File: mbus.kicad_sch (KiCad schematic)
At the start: 7 parts

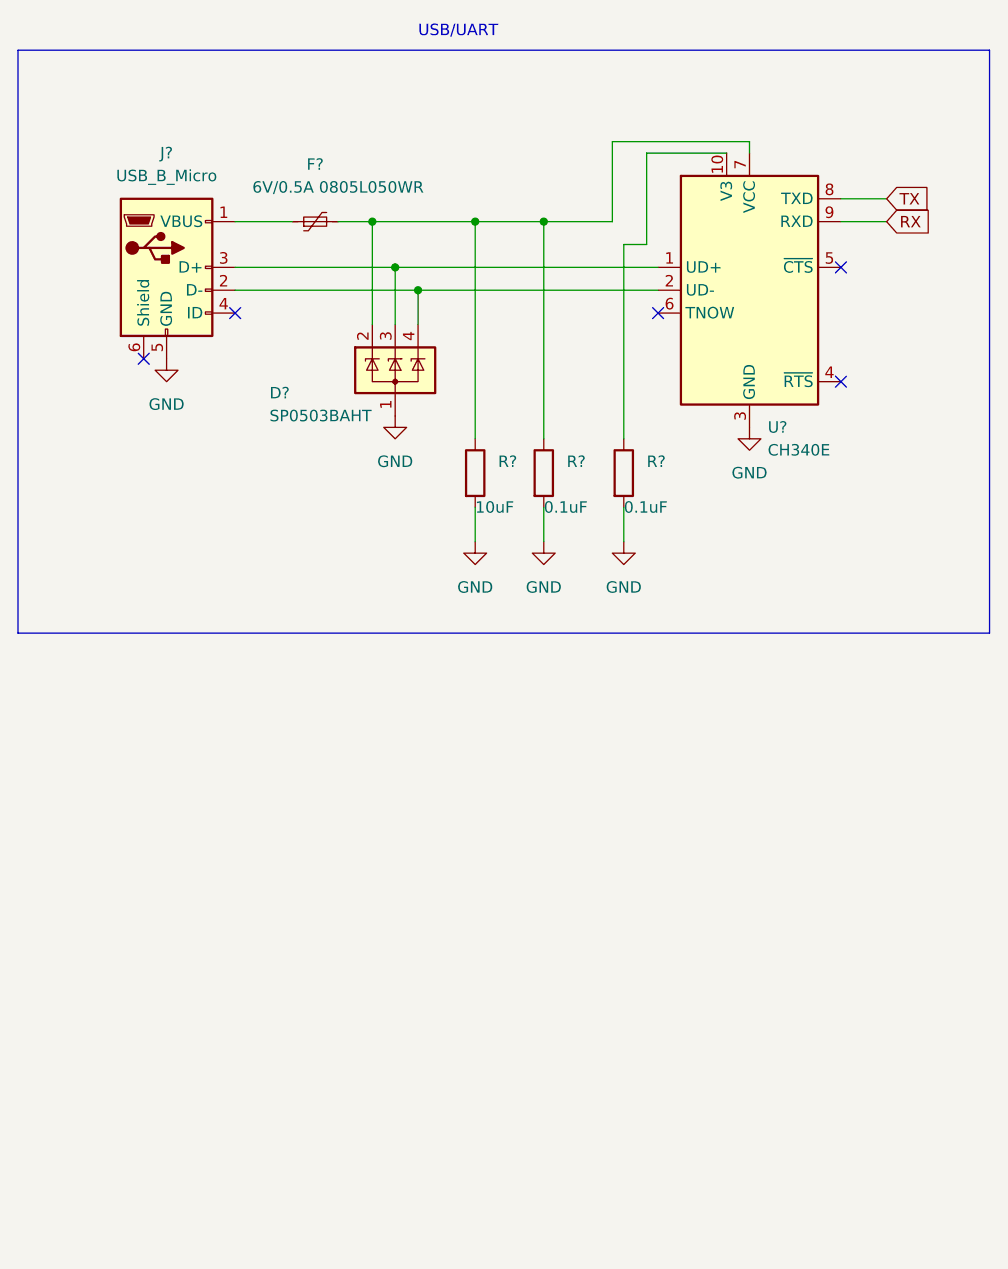
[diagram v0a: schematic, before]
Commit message: mbus driving logic WIP
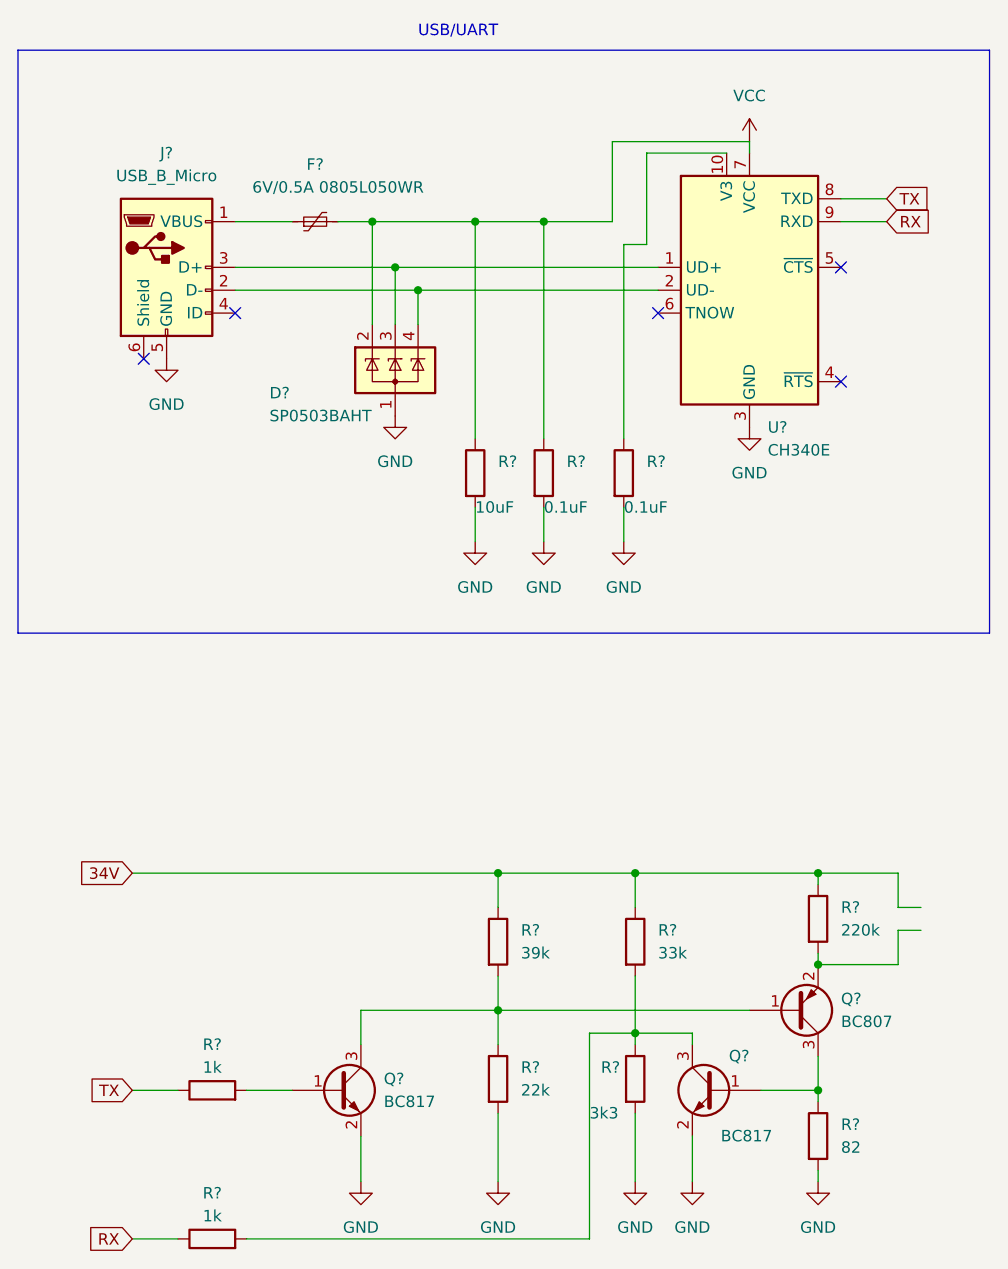
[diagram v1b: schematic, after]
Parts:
- added Q? (x2): BC817, Package_TO_SOT_SMD:SOT-23, symbol Transistor_BJT:BC817
- added Q?: BC807, Package_TO_SOT_SMD:SOT-23, symbol Transistor_BJT:BC807
- added R?: 220k, symbol Device:R
- added R?: 3k3, symbol Device:R
- added R?: 39k, symbol Device:R
- added R?: 22k, symbol Device:R
- added R?: 33k, symbol Device:R
- added R?: 82, symbol Device:R
- added R? (x2): 1k, symbol Device:R
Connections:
- net GND: now also Q?.2 (E), Q?.2 (E), R?.2, R?.2, R?.2
- net RX: now also R?.1
- net TX: now also R?.1
- net VCC: now reaches D?.2 (K), F?.2, R?.1, R?.1, U?.7 (VCC)
- new net: Q?.2 (E), R?.2
- new net: Q?.3 (C), R?.1, R?.2, R?.2
- new net: Q?.1 (B), Q?.3 (C), R?.1, R?.2
- new net: Q?.1 (B), Q?.3 (C), R?.1
- new net: Q?.1 (B), R?.2
- new net 34V: R?.1, R?.1, R?.1

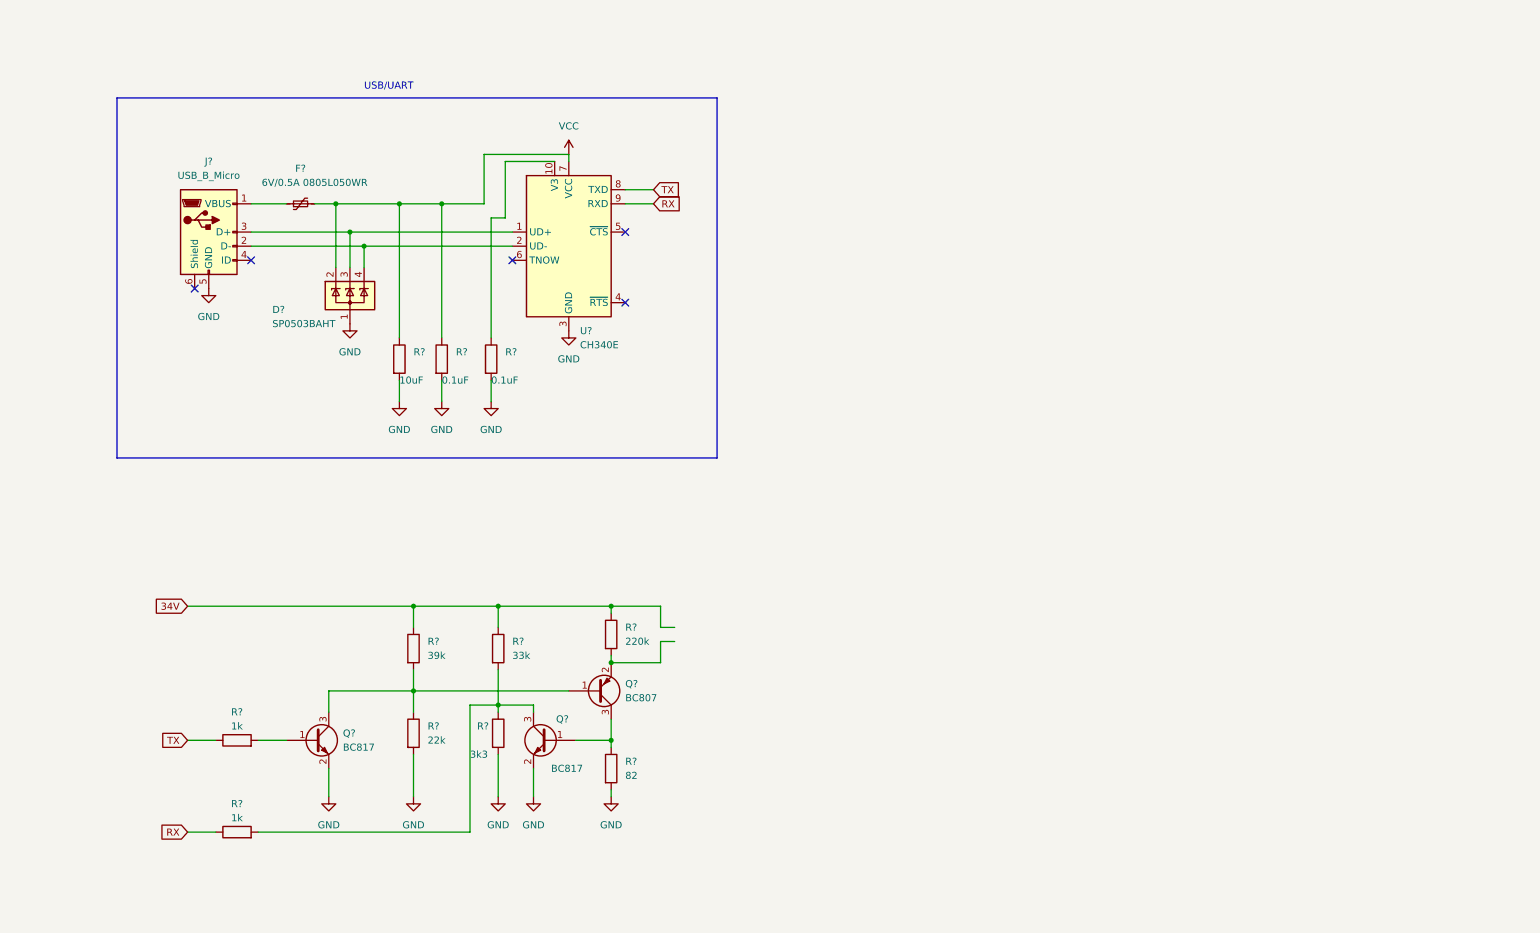
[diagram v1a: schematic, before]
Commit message: Added boost converter, protection components for mbus
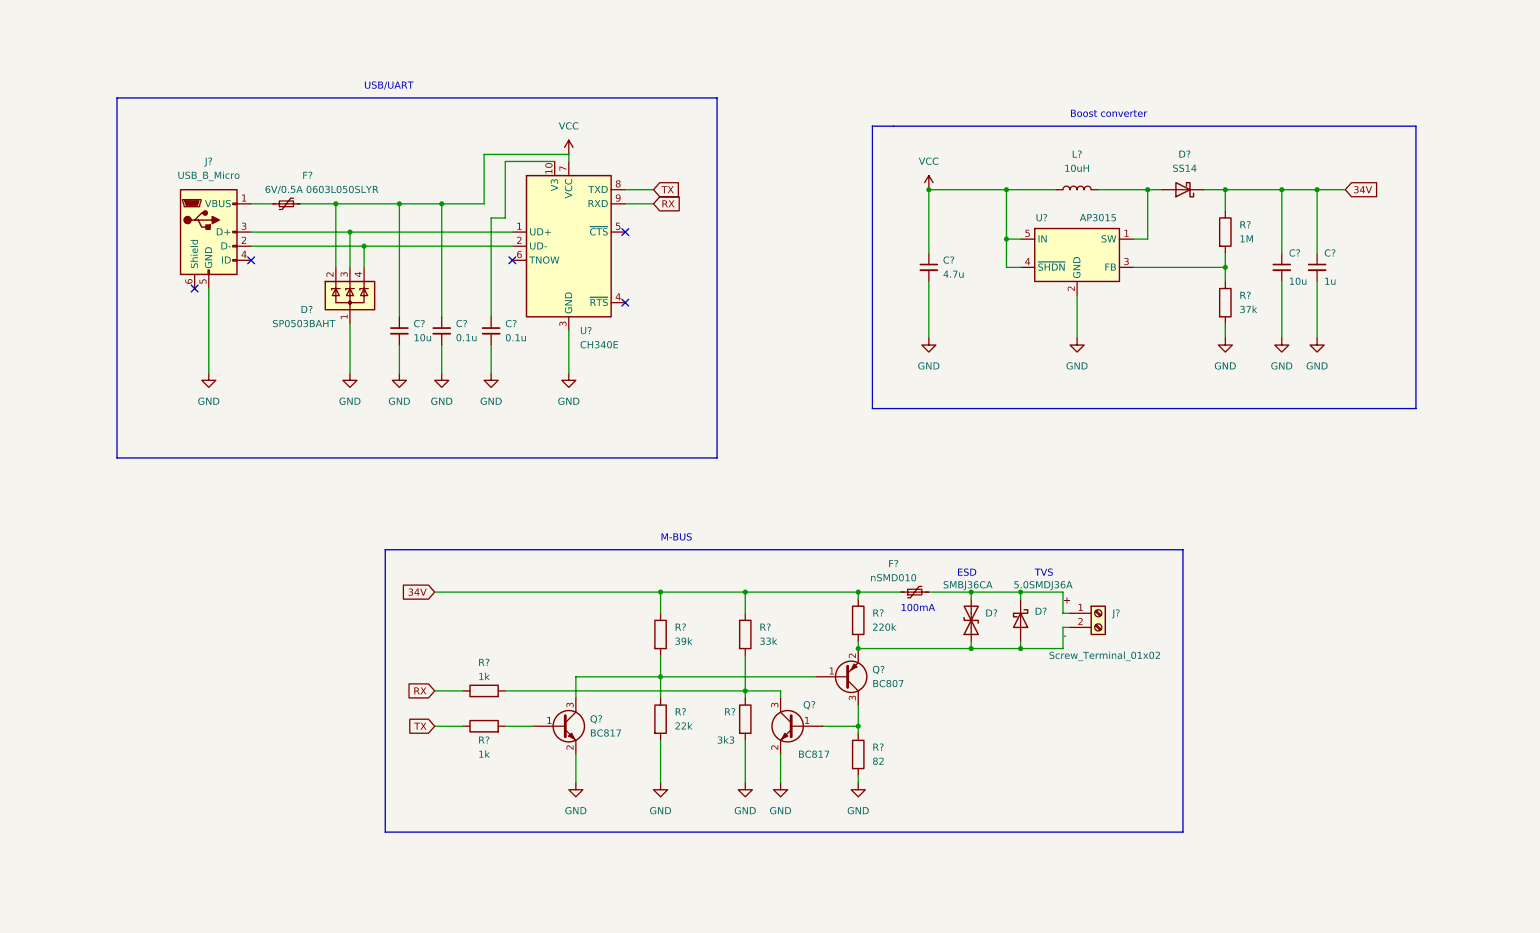
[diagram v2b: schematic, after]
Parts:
- removed R?: 10uF, symbol Device:R
- removed R? (x2): 0.1uF, symbol Device:R
- added C?: 4.7u, symbol Device:C_Small
- added C? (x2): 0.1u, symbol Device:C_Small
- added C? (x2): 10u, symbol Device:C_Small
- added C?: 1u, symbol Device:C_Small
- added D?: SMBJ36CA, symbol Device:D_TVS
- added D?: 5.0SMDJ36A, symbol Device:D_Schottky
- added D?: SS14, symbol Device:D_Schottky
- added F?: nSMD010, symbol Device:Polyfuse_Small
- added J?: Screw_Terminal_01x02, symbol Connector:Screw_Terminal_01x02
- added L?: 10uH, symbol Device:L
- added R?: 37k, symbol Device:R
- added R?: 1M, symbol Device:R
- added U?: AP3015, Package_TO_SOT_SMD:SOT-23-5, symbol mbus_lib:AP3015
- F?: value 6V/0.5A 0805L050WR -> 6V/0.5A 0603L050SLYR
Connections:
- net 34V: now also C?.1, C?.1, D?.1 (K), F?.1, R?.1
- net GND: now also C?.2, C?.2, C?.2, C?.2, C?.2, C?.2, R?.2, U?.2 (GND)
- net VCC: now also C?.1, C?.1, C?.1, L?.1, U?.4 (~{SHDN}), U?.5 (IN)
- net -: now reaches Q?.2 (E), R?.2
- net -: now also D?.1 (A1), D?.2 (A), J?.2 (Pin_2)
- net at U?.10 (V3): now also C?.1
- new net: D?.2 (A), L?.2, U?.1 (SW)
- new net: R?.1, R?.2, U?.3 (FB)
- new net +: D?.1 (K), D?.2 (A2), F?.2, J?.1 (Pin_1)
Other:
- note added: "100mA"
- note added: "Boost converter"
- note added: "ESD"
- note added: "M-BUS"
- note added: "TVS"
- moved on the sheet: F?, Q?, R?

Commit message: Generated designators
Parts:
- F1: renamed from F?; value 6V/0.5A 0603L050SLYR -> 0603L050SLYR
- J2: renamed from J?; value Screw_Terminal_01x02 -> MBUS
- gave numbers to parts that had none: 28
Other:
- note added: "500mA"

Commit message: Replaced 500mA VBUS fuse with 200mA, changed MBUS circuit to work with 5V logic
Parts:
- C1, C2, C3, C4, C5, C6: footprint (none) -> Capacitor_SMD:C_0603_1608Metric
- F1: value 0603L050SLYR -> (none)
- R2: value 1k -> (none)
- R6: value 3k3 -> (none)
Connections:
- net VCC renamed +5V
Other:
- note added: "200mA"
- note added: "R2: 1k"
- note added: "R6: 3k3"
- note added: "Replace these for 3.3V logic levels:"
- note removed: "500mA"

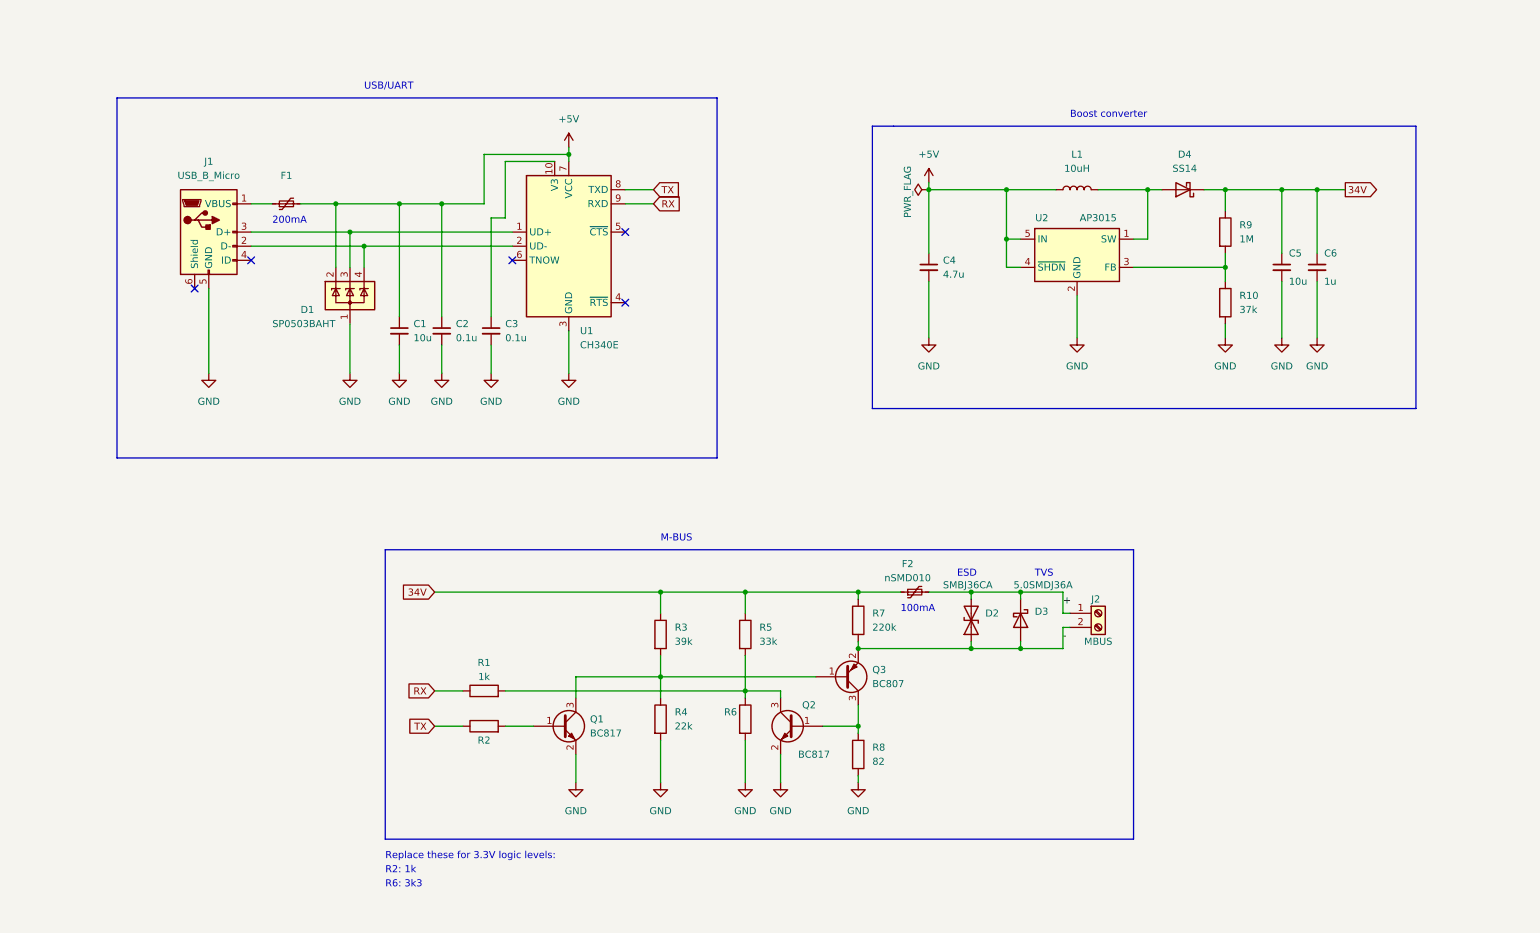
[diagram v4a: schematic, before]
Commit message: Added part numbers, schematic to readme and symbol for mbus power rail
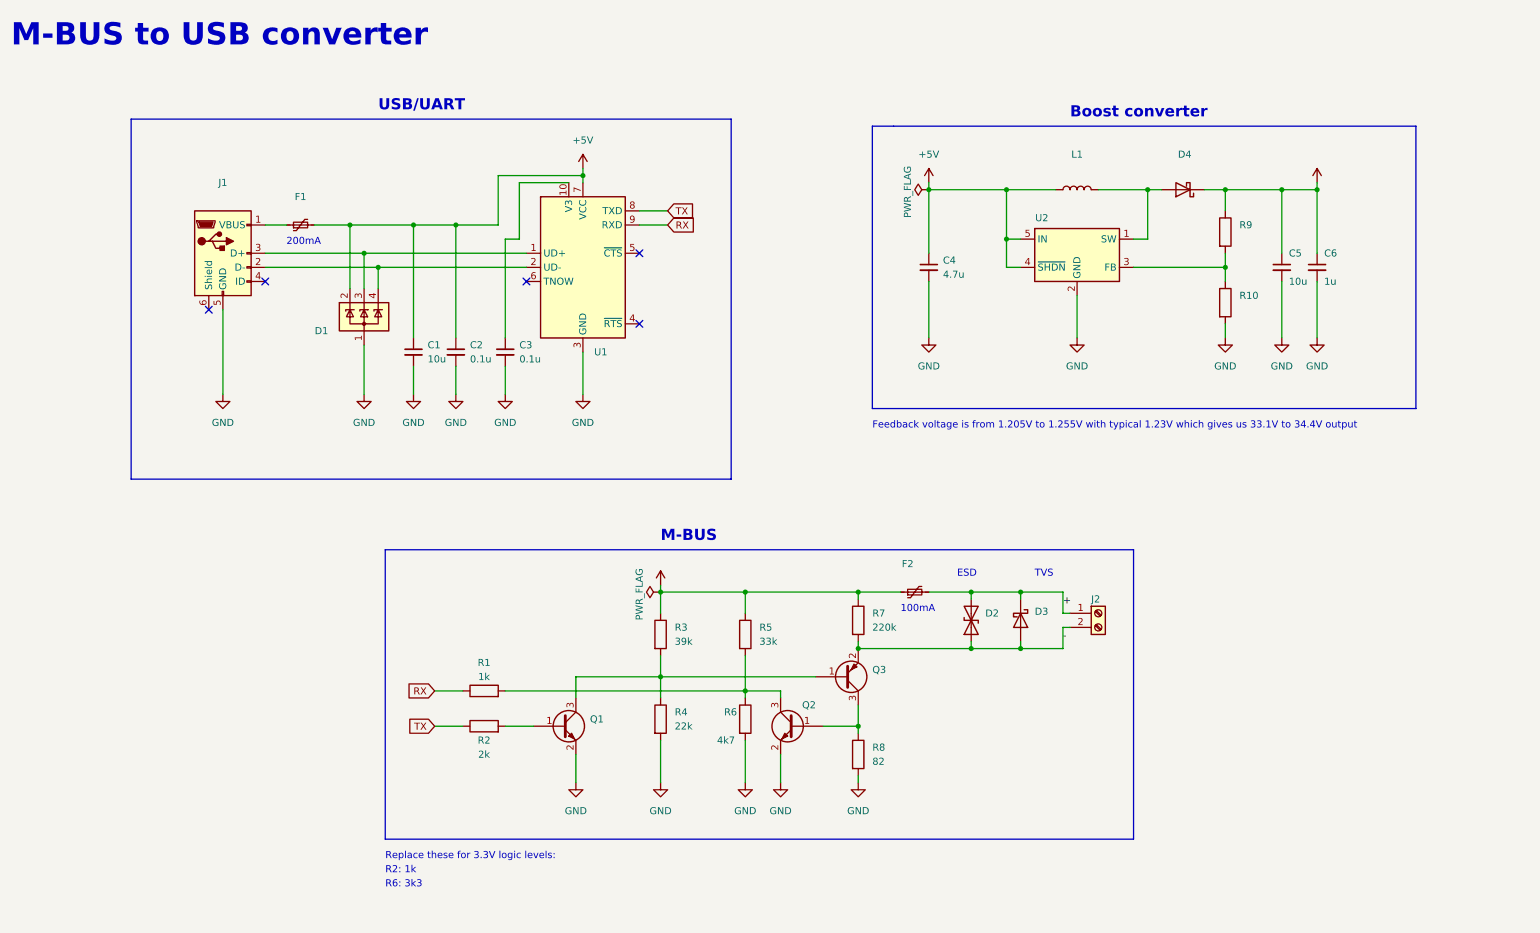
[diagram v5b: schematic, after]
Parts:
- D1: value SP0503BAHT -> (none); footprint Package_TO_SOT_SMD:SOT-143 -> (none); LCSC (none) -> C7074
- D2: value SMBJ36CA -> (none); LCSC (none) -> C83326
- D3: value 5.0SMDJ36A -> (none); LCSC (none) -> C522690
- D4: value SS14 -> (none); LCSC (none) -> C190475
- F1: LCSC (none) -> C2760255
- F2: value nSMD010 -> (none); LCSC (none) -> C70065
- J1: value USB_B_Micro -> (none); LCSC (none) -> C132563
- J2: value MBUS -> (none); LCSC (none) -> C474881
- L1: value 10uH -> (none); LCSC (none) -> C408412
- Q1, Q2: value BC817 -> (none); footprint Package_TO_SOT_SMD:SOT-23 -> (none); LCSC (none) -> C604682
- Q3: value BC807 -> (none); footprint Package_TO_SOT_SMD:SOT-23 -> (none); LCSC (none) -> C82369
- R1, R3, R4, R5, R7, R8: footprint (none) -> Resistor_SMD:R_0603_1608Metric
- R10: value 37k -> (none)
- R2: value (none) -> 2k; footprint (none) -> Resistor_SMD:R_0603_1608Metric
- R6: value (none) -> 4k7; footprint (none) -> Resistor_SMD:R_0603_1608Metric
- R9: value 1M -> (none)
- U1: value CH340E -> (none); footprint Package_SO:MSOP-10_3x3mm_P0.5mm -> (none); LCSC (none) -> C99652
- U2: value AP3015 -> (none); footprint Package_TO_SOT_SMD:SOT-23-5 -> (none); LCSC (none) -> C151334
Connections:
- net 34V renamed +34V
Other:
- note added: "Feedback voltage is from 1.205V to 1.255V with typical 1.23V which gives us 33.1V to 34.4V output"
- note added: "M-BUS to USB converter"
- moved on the sheet: C1, C2, C3, D1, F1, J1, U1
